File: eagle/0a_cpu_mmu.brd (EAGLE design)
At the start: 9 parts

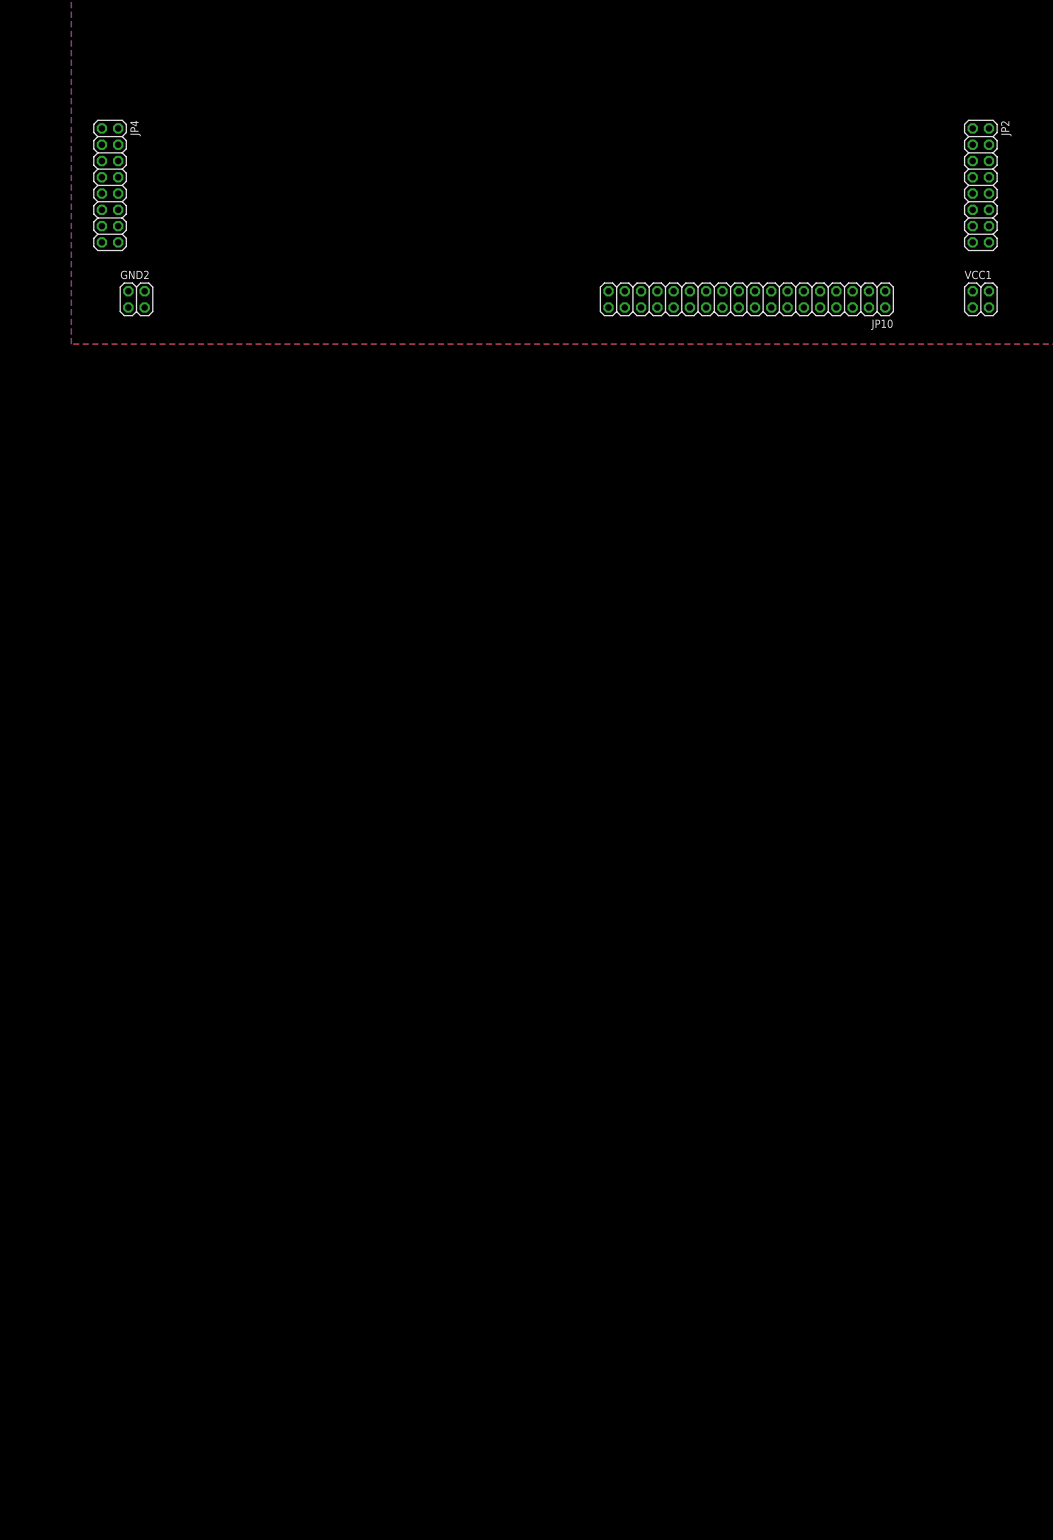
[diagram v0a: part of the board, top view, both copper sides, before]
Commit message: Parts library updated (added fast SRAM), MMU board half complete
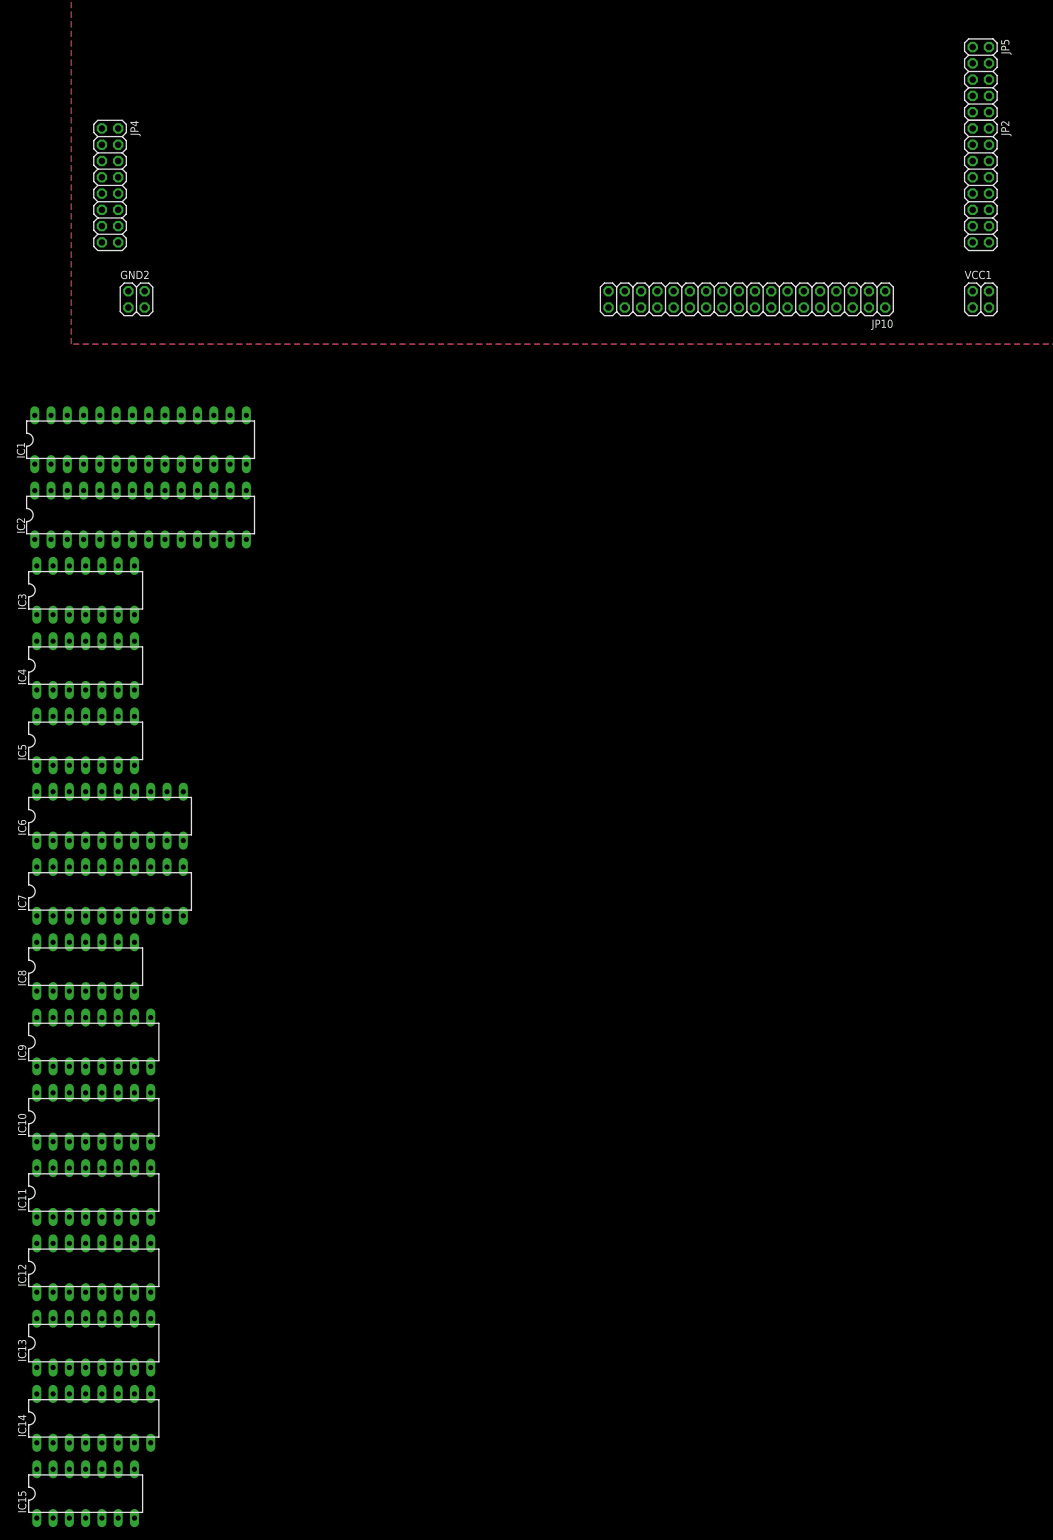
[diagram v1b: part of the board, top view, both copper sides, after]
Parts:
- added IC1, IC2: MT5C6408, dawid:DIL28-3
- added IC10, IC11, IC12, IC13, IC14, IC9: 74LS157N, 74xx-eu:DIL16
- added IC15: 74LS04N, 74xx-eu:DIL14
- added IC3: 74LS27N, 74xx-eu:DIL14
- added IC4: 74LS20N, 74xx-eu:DIL14
- added IC5: 74LS08N, 74xx-eu:DIL14
- added IC6, IC7: 74LS245N, 74xx-eu:DIL20
- added IC8: 74LS32N, 74xx-eu:DIL14
- added JP5: (no value), pinhead:2X05
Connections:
- new net /ENPTAB: IC14.14, IC6.1, IC7.1, IC8.6
- new net /LDPTAB: IC1.27, IC2.27, IC8.3
- new net /PTAB: IC13.1, IC14.1, IC4.6, IC8.1, IC8.12, IC8.4, IC8.9
- new net N$1: IC3.12, IC4.1
- new net N$10: IC1.17, IC10.5, IC6.7
- new net N$11: IC1.18, IC10.11, IC6.8
- new net N$12: IC1.19, IC10.14, IC6.9
- new net N$13: IC2.11, IC7.2
- new net N$14: IC2.12, IC7.3
- new net N$15: IC2.13, IC7.4
- new net N$16: IC2.15, IC7.5
- new net N$17: IC2.16, IC7.6
- new net N$18: IC2.17, IC7.7
- new net N$19: IC2.18, IC7.8
- new net N$2: IC3.6, IC4.2
- new net N$20: IC2.19, IC7.9
- new net N$21: IC1.10, IC13.4, IC2.10
- new net N$22: IC1.9, IC13.7, IC2.9
- new net N$23: IC1.8, IC13.9, IC2.8
- new net N$24: IC1.7, IC13.12, IC2.7
- new net N$25: IC1.6, IC14.4, IC2.6
- new net N$26: IC1.5, IC14.7, IC2.5
- new net N$27: IC1.26, IC7.19, IC8.8
- new net N$28: IC2.26, IC6.19, IC8.11
- new net N$29: IC1.22, IC14.12, IC2.22
- new net N$3: IC3.8, IC4.4
- new net N$30: IC15.2, IC8.10
- new net N$4: IC4.5, IC5.3
- new net N$5: IC1.11, IC6.2, IC9.2
- new net N$6: IC1.12, IC6.3, IC9.5
- new net N$7: IC1.13, IC6.4, IC9.11
- new net N$8: IC1.15, IC6.5, IC9.14
- new net N$9: IC1.16, IC10.2, IC6.6
- new net PABUS12: JP5.1
- new net PABUS13: JP5.2
- new net PABUS14: JP5.3
- new net PABUS15: JP5.4
- new net PABUS16: JP5.5
- new net PABUS17: JP5.6
- new net PABUS18: JP5.7
- new net PABUS19: JP5.8
- new net PABUS20: JP5.9
- new net PABUS21: JP5.10
- new net VCC: IC1.28, IC10.16, IC11.16, IC12.16, IC13.16, IC14.16, IC15.14, IC2.28, IC3.14, IC4.14, IC5.14, IC6.20, IC7.20, IC8.14, IC9.16
- net /ENMEM: now also IC8.5
- net /FS: now also IC14.6, IC3.11
- net /LDMEM: now also IC8.2
- net ABUS0: now also IC15.1, IC8.13
- net ABUS1: now also IC13.2
- net ABUS10: now also IC3.13
- net ABUS11: now also IC3.3
- net ABUS12: now also IC13.3, IC3.4
- net ABUS13: now also IC13.6, IC3.5
- net ABUS14: now also IC13.10, IC3.9
- net ABUS15: now also IC13.13, IC3.10
- net ABUS2: now also IC13.5
- net ABUS3: now also IC13.11
- net ABUS4: now also IC13.14
- net ABUS5: now also IC14.2
- net ABUS6: now also IC14.5
- net ABUS7: now also IC5.1
- net ABUS8: now also IC3.1
- net ABUS9: now also IC3.2
- net DBUS0: now also IC6.18, IC7.18
- net DBUS1: now also IC6.17, IC7.17
- net DBUS2: now also IC6.16, IC7.16
- net DBUS3: now also IC6.15, IC7.15
- net DBUS4: now also IC6.14, IC7.14
- net DBUS5: now also IC6.13, IC7.13
- net DBUS6: now also IC6.12, IC7.12
- net DBUS7: now also IC6.11, IC7.11
- net GND: now also IC1.14, IC1.2, IC1.20, IC1.21, IC1.23, IC1.24, IC1.25, IC1.3, IC1.4, IC10.10, IC10.13, IC10.3, IC10.6, IC10.8, IC11.8, IC12.8, IC13.15, IC13.8, IC14.13, IC14.15, IC14.8, IC15.7, IC2.14, IC2.2, IC2.20, IC2.21, IC2.23, IC2.24, IC2.25, IC2.3, IC2.4, IC3.7, IC4.7, IC5.7, IC6.10, IC7.10, IC8.7, IC9.10, IC9.13, IC9.3, IC9.6, IC9.8
- net MEMSEG: now also IC14.3, IC5.2

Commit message: MMU schematics update
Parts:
- added IC16: 74LS04N, 74xx-eu:DIL14
- added IC17: 74LS32N, 74xx-eu:DIL14
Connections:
- new net /ENMEMX: IC12.4
- new net /LDMEMX: IC12.7
- new net FIO: IC16.1, IC2.17, IC7.7
- new net FPRESENT: IC17.12, IC2.19, IC7.9
- new net FWRITABLE: IC17.9, IC2.18, IC7.8
- new net N$31: IC12.10, IC17.6
- new net N$32: IC12.13, IC17.3
- new net N$33: IC17.4, IC17.8
- new net N$34: IC17.1, IC17.11
- net +5V: now also IC11.10, IC12.11, IC12.14, IC12.2, IC12.5
- net /ENMEM: now also IC12.3, IC17.2
- net /FP: now also IC10.1, IC11.1, IC17.10, IC17.13, IC9.1
- net /IO: now also IC11.9
- net /LDMEM: now also IC17.5
- net /NP_FAULT: now also IC12.12
- net /PTAB: now also IC12.1; no longer IC13.1, IC14.1, IC4.6, IC8.1, IC8.12, IC8.4, IC8.9
- net /WR_FAULT: now also IC12.9
- net GND: now also IC10.15, IC11.15, IC11.3, IC11.6, IC12.15, IC16.7, IC17.7, IC9.15
- net N$13: now also IC11.2
- net N$14: now also IC11.5
- net N$18: now also IC11.11, IC16.2; no longer IC2.17, IC7.7
- net N$19: now also IC13.1, IC14.1, IC4.6, IC8.1, IC8.12, IC8.4, IC8.9; no longer IC2.18, IC7.8
- net N$20: now also IC12.6; no longer IC2.19, IC7.9
- net PABUS12: now also IC9.4
- net PABUS13: now also IC9.7
- net PABUS14: now also IC9.9
- net PABUS15: now also IC9.12
- net PABUS16: now also IC10.4
- net PABUS17: now also IC10.7
- net PABUS18: now also IC10.9
- net PABUS19: now also IC10.12
- net PABUS20: now also IC11.4
- net PABUS21: now also IC11.7
- net VCC: now also IC16.14, IC17.14

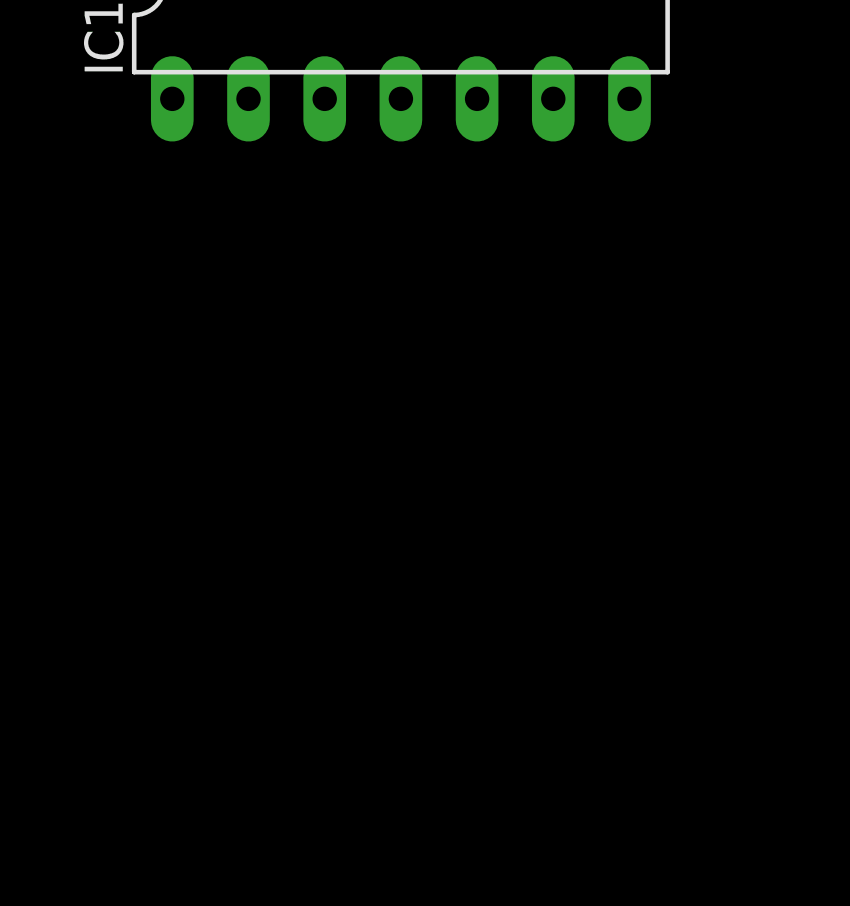
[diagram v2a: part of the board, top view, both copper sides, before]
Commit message: Updates to MMU faults generation circuit
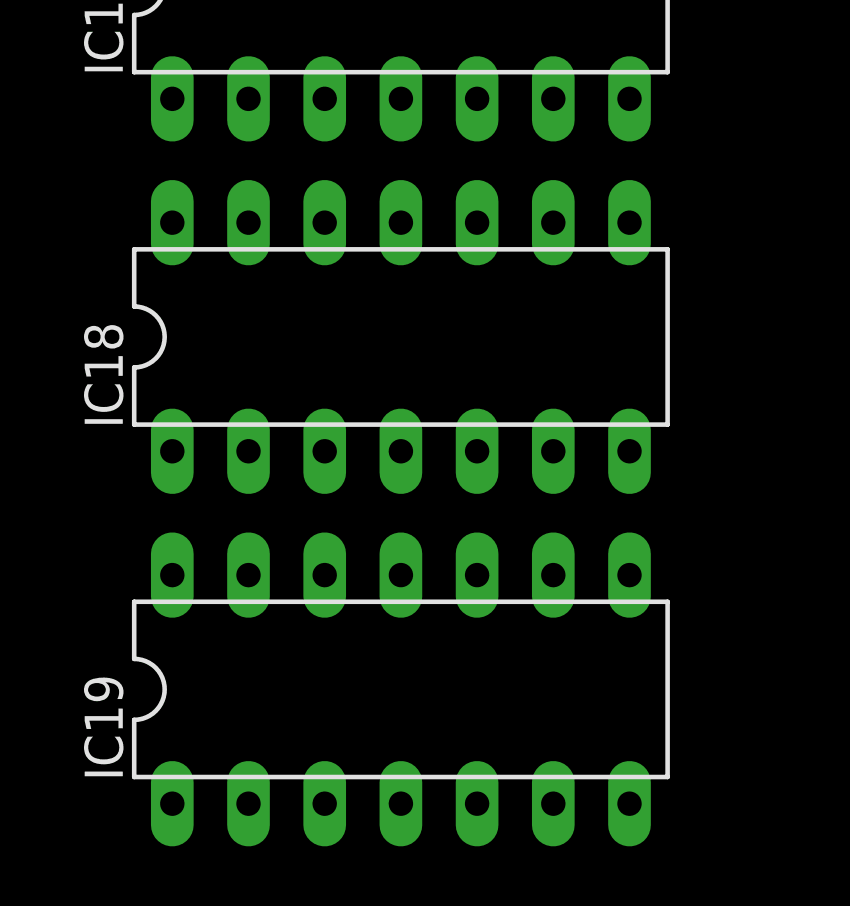
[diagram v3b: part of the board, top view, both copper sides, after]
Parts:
- added IC18: 74LS00N, 74xx-eu:DIL14
- added IC19: 74LS32N, 74xx-eu:DIL14
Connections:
- new net N$35: IC17.1, IC18.1, IC19.3
- net /ENMEM: now also IC5.5; no longer IC17.2
- net /FP: now also IC19.2; no longer IC17.10
- net /LDMEM: now also IC17.9, IC5.4
- net /PTAB: now also IC13.1, IC14.1, IC4.6, IC8.1, IC8.12, IC8.4, IC8.9
- net FPRESENT: now also IC19.1; no longer IC17.12
- net FWRITABLE: now also IC17.12; no longer IC17.9
- net GND: now also IC11.13, IC11.14, IC14.10, IC14.11, IC18.7, IC19.7
- net N$19: now also IC17.2, IC5.6; no longer IC13.1, IC14.1, IC4.6, IC8.1, IC8.12, IC8.4, IC8.9
- net N$20: now also IC17.8
- net N$33: now also IC17.10, IC18.3; no longer IC17.4, IC17.8
- net N$34: now also IC17.4, IC18.2; no longer IC17.1
- net VCC: now also IC18.14, IC19.14

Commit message: More MMU changes, added PPREG
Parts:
- removed IC16: 74LS04N, 74xx-eu:DIL14
- added IC20: 74LS02N, 74xx-eu:DIL14
- added IC21: 74LS374N, 74xx-eu:DIL20
- moved IC17 289.8 mm to (87.9, 74.0)
- moved IC18 289.8 mm to (87.9, 62.2)
- moved IC19 289.8 mm to (87.9, 50.5)
- moved IC10 204.3 mm to (56.8, 76.5)
- moved IC11 204.3 mm to (56.8, 64.8)
- moved IC12 204.3 mm to (56.8, 53.0)
- moved IC13 204.3 mm to (56.8, 41.3)
- moved IC9 204.3 mm to (56.8, 88.3)
- moved IC14 204.3 mm to (56.8, 29.5)
- moved IC15 204.3 mm to (55.6, 17.8)
- moved IC6 196.6 mm to (128.6, 80.0), turned to 270 degrees
- moved IC7 181.1 mm to (128.6, 47.9), turned to 270 degrees
- moved IC1 136.8 mm to (114.0, 74.9), turned to 90 degrees
- moved IC3 132.1 mm to (29.8, 90.8)
- moved IC4 132.1 mm to (29.8, 79.1)
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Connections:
- removed net N$3: IC3.8, IC4.4
- new net /PPREG: IC19.13, IC4.8, IC5.10
- new net N$37: IC3.8, IC4.12, IC4.4
- new net N$39: IC12.1, IC5.8
- new net N$40: IC18.8, IC19.10
- new net N$41: IC19.8, IC21.11
- new net N$42: IC19.11, IC21.1
- net +5V: now also IC21.17, IC21.18
- net /ENMEM: now also IC19.12
- net /FS: now also IC20.6, IC21.14
- net /PTAB: now also IC5.9; no longer IC12.1
- net ABUS12: now also IC21.3
- net ABUS13: now also IC21.4
- net ABUS14: now also IC21.7
- net ABUS15: now also IC21.8
- net ABUS7: now also IC20.5
- net CLK0A: now also IC19.9
- net DBUS0: now also IC21.2
- net DBUS1: now also IC21.5
- net DBUS2: now also IC21.6
- net DBUS3: now also IC21.9
- net DBUS4: now also IC21.12
- net DBUS5: now also IC21.15
- net DBUS6: now also IC21.16
- net DBUS7: now also IC21.19
- net FIO: now also IC15.3; no longer IC16.1
- net GND: now also IC20.7, IC21.10; no longer IC16.7
- net MEMSEG: now also IC21.13
- net N$1: now also IC4.9
- net N$18: now also IC15.4; no longer IC16.2
- net N$2: now also IC4.10
- net N$31: now also IC18.9
- net N$32: now also IC18.10
- net VCC: now also IC20.14, IC21.20; no longer IC16.14

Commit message: Removal of PPC started
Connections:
- removed net /LDPPC: JP10.11
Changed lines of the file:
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@@
 <contactref element="JP10" pad="1"/>
-</signal>
-<signal name="/LDPPC">
-<contactref element="JP10" pad="11"/>
 </signal>
 <signal name="PROT">
